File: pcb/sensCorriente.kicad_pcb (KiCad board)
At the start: 2 copper layers, 29 parts, among them J1 I_in, J2 USB, J3 SD-CON, J4 DB9, P1 LPCXpresso, SW1 CALIB, U1 ACS713, U2 MAX232

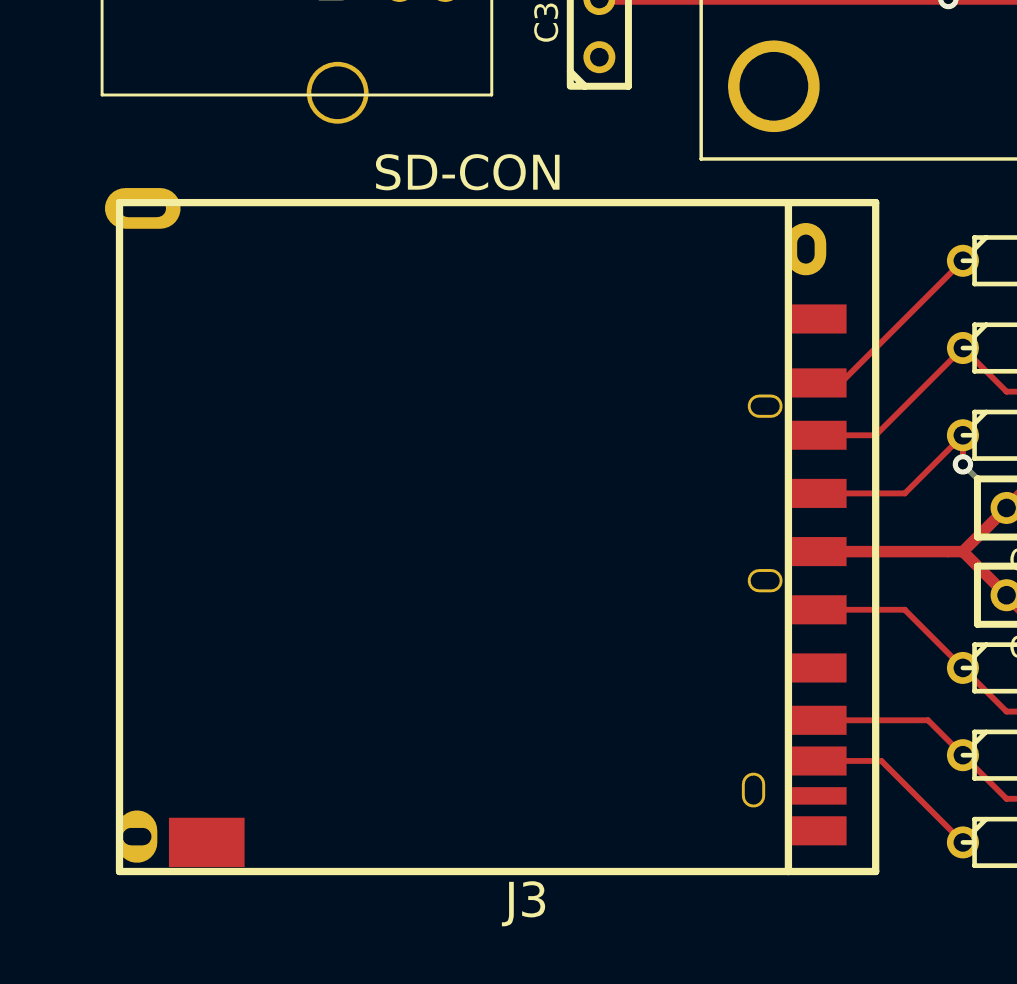
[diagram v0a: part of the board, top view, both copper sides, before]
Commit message: Se realizaron cambios en el esquematico. Revisar ERC.
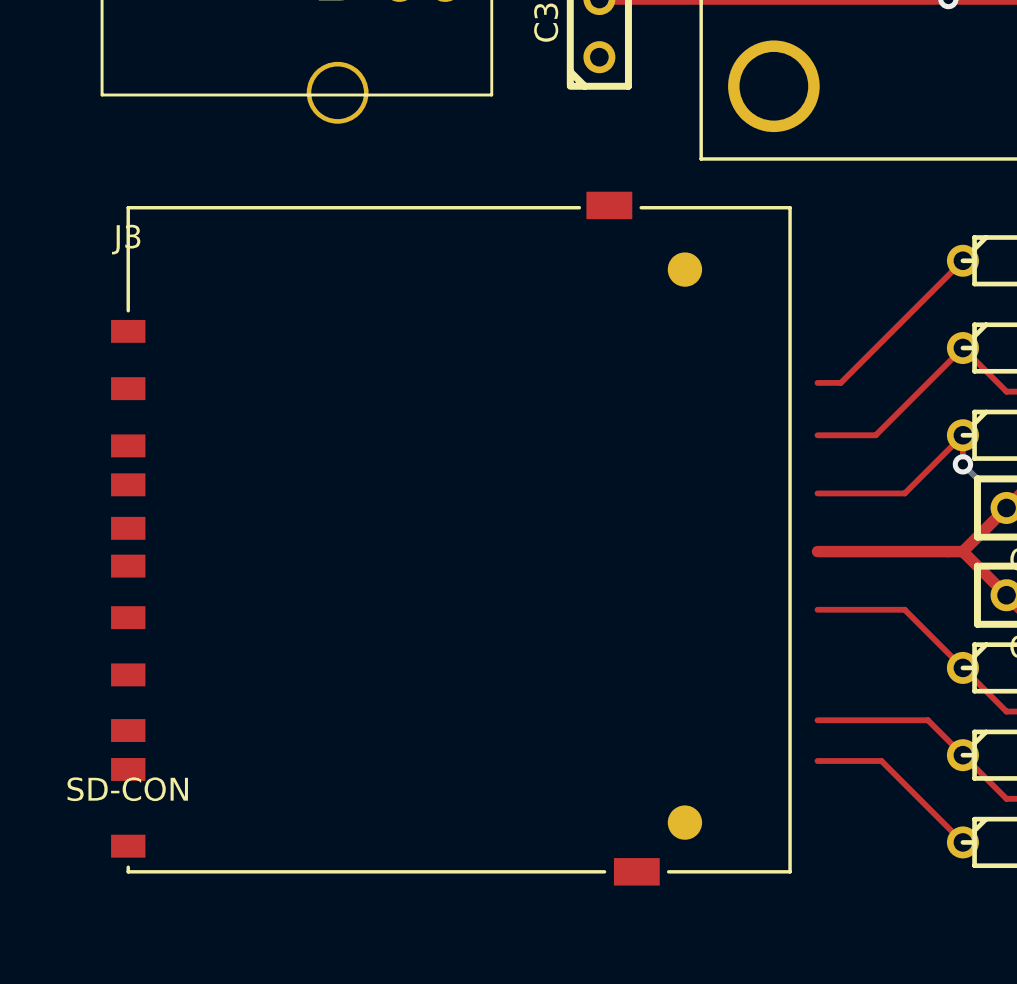
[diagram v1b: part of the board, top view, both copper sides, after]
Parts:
- J3: footprint SDCARD-REVERSE -> SD-CARD
- moved J3 30.4 mm to (124.2, 170.4), turned to 0 degrees
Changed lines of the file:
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@@
 (kicad_pcb (version 3) (host pcbnew "(2013-07-07 BZR 4022)-stable")
   (general
-    (links 90)
-    (no_connects 32)
+    (links 87)
+    (no_connects 36)
     (area 122.745499 115.443 308.381401 187.8584)
     (thickness 1.6)
@@
   )
   (setup
-    (last_trace_width 0.5)
+    (last_trace_width 0.254)
     (user_trace_width 0.5)
     (user_trace_width 1)
@@
     )
   )
-  (module SDCARD-REVERSE (layer F.Cu)
-    (at 154.305 166.37 180)
-    (fp_text reference J3 (at 12.7 -20.32 180) (layer F.SilkS)
-      (effects (font (size 1.524 1.524) (thickness 0.3048)))
-    )
-    (fp_text value SD-CON (at 15.24 11.43 180) (layer F.SilkS)
-      (effects (font (size 1.524 1.524) (thickness 0.3048)))
-    )
-    (fp_line (start 1.27 -19.05) (end -2.54 -19.05) (layer F.SilkS) (width 0.3175))
-    (fp_line (start -2.54 -19.05) (end -2.54 10.16) (layer F.SilkS) (width 0.3175))
-    (fp_line (start -2.54 10.16) (end 1.27 10.16) (layer F.SilkS) (width 0.3175))
-    (fp_line (start 30.48 -19.05) (end 1.27 -19.05) (layer F.SilkS) (width 0.3175))
-    (fp_line (start 1.27 -19.05) (end 1.27 10.16) (layer F.SilkS) (width 0.3175))
-    (fp_line (start 30.48 10.16) (end 1.27 10.16) (layer F.SilkS) (width 0.3175))
-    (fp_line (start 30.48 -19.05) (end 30.48 10.16) (layer F.SilkS) (width 0.3175))
-    (pad 9 smd rect (at 0 5.08 180) (size 2.54 1.27)
-      (layers F.Cu F.Paste F.Mask)
-      (net 21 GND)
-    )
-    (pad 1 smd rect (at 0 2.286 180) (size 2.54 1.27)
-      (layers F.Cu F.Paste F.Mask)
-      (net 23 N-0000025)
-    )
-    (pad 2 smd rect (at 0 0 180) (size 2.54 1.27)
-      (layers F.Cu F.Paste F.Mask)
-      (net 17 /SD_SSEL)
-    )
-    (pad 3 smd rect (at 0 -2.54 180) (size 2.54 1.27)
-      (layers F.Cu F.Paste F.Mask)
-      (net 16 /SD_MOSI)
-    )
-    (pad 4 smd rect (at 0 -5.08 180) (size 2.54 1.27)
-      (layers F.Cu F.Paste F.Mask)
-      (net 1 +3.3V)
-    )
-    (pad 5 smd rect (at 0 -7.62 180) (size 2.54 1.27)
-      (layers F.Cu F.Paste F.Mask)
-      (net 14 /SD_CLK)
-    )
-    (pad 6 smd rect (at 0 -10.16 180) (size 2.54 1.27)
-      (layers F.Cu F.Paste F.Mask)
-      (net 21 GND)
-    )
-    (pad 10 smd rect (at 0 -15.748 180) (size 2.54 0.762)
-      (layers F.Cu F.Paste F.Mask)
-      (net 21 GND)
-    )
-    (pad 8 smd rect (at 0 -14.224 180) (size 2.54 1.27)
-      (layers F.Cu F.Paste F.Mask)
-      (net 22 N-0000024)
-    )
-    (pad 11 smd rect (at 0 -17.272 180) (size 2.54 1.27)
-      (layers F.Cu F.Paste F.Mask)
-      (net 21 GND)
-    )
-    (pad 13 thru_hole oval (at 2.794 -15.494 180) (size 1.016 1.524) (drill oval 0.762 1.27)
-      (layers *.Cu *.Mask F.SilkS)
-    )
-    (pad 15 thru_hole oval (at 2.286 1.27 180) (size 1.524 1.016) (drill oval 1.27 0.762)
-      (layers *.Cu *.Mask F.SilkS)
-    )
-    (pad 16 thru_hole oval (at 0.508 8.128 180) (size 1.778 2.286) (drill oval 0.762 1.27)
-      (layers *.Cu *.Mask F.SilkS)
-    )
-    (pad 14 thru_hole oval (at 2.286 -6.35 180) (size 1.524 1.016) (drill oval 1.27 0.762)
-      (layers *.Cu *.Mask F.SilkS)
-    )
-    (pad 18 thru_hole oval (at 29.718 -17.526 180) (size 1.778 2.286) (drill oval 1.27 0.762)
-      (layers *.Cu *.Mask F.SilkS)
-    )
-    (pad 17 thru_hole oval (at 29.464 9.906 180) (size 3.302 1.778) (drill oval 2.032 0.762)
-      (layers *.Cu *.Mask F.SilkS)
-    )
-    (pad 7 smd rect (at 0 -12.446 180) (size 2.54 1.27)
-      (layers F.Cu F.Paste F.Mask)
-      (net 15 /SD_MISO)
-    )
-    (pad 12 smd rect (at 26.67 -17.78 180) (size 3.302 2.159)
-      (layers F.Cu F.Paste F.Mask)
-      (net 21 GND)
-    )
-  )
   (module RV2X4 (layer F.Cu)
     (at 258.445 124.46 270)
@@
       (scale (xyz 1 1 1))
       (rotate (xyz 0 0 0))
+    )
+  )
+  (module SD-CARD (layer F.Cu)
+    (at 124.206 170.434)
+    (fp_text reference J3 (at 0 -12.7) (layer F.SilkS)
+      (effects (font (size 1 1) (thickness 0.15)))
+    )
+    (fp_text value SD-CON (at 0 11.43) (layer F.SilkS)
+      (effects (font (size 1 1) (thickness 0.15)))
+    )
+    (fp_line (start 19.7 -14) (end 0 -14) (layer F.SilkS) (width 0.15))
+    (fp_line (start 28.9 15) (end 23.6 15) (layer F.SilkS) (width 0.15))
+    (fp_line (start 20.8 15) (end 0 15) (layer F.SilkS) (width 0.15))
+    (fp_line (start 0 15) (end 0 14.8) (layer F.SilkS) (width 0.15))
+    (fp_line (start 0 -14) (end 0 -9.5) (layer F.SilkS) (width 0.15))
+    (fp_line (start 28.9 -14) (end 28.9 15) (layer F.SilkS) (width 0.15))
+    (fp_line (start 22.4 -14) (end 28.9 -14) (layer F.SilkS) (width 0.15))
+    (pad 3 smd rect (at 0 0) (size 1.5 1)
+      (layers F.Cu F.Paste F.Mask)
+      (net 16 /SD_MOSI)
+    )
+    (pad 9 smd rect (at 0 -8.6) (size 1.5 1)
+      (layers F.Cu F.Paste F.Mask)
+      (net 21 GND)
+    )
+    (pad 2 smd rect (at 0 -3.6) (size 1.5 1)
+      (layers F.Cu F.Paste F.Mask)
+      (net 17 /SD_SSEL)
+    )
+    (pad CD smd rect (at 0 -1.9) (size 1.5 1)
+      (layers F.Cu F.Paste F.Mask)
+    )
+    (pad "" np_thru_hole circle (at 24.31 -11.3) (size 1.5 1.5)
+      (layers *.Cu *.Mask F.SilkS)
+    )
+    (pad 5 smd rect (at 0 3.9) (size 1.5 1)
+      (layers F.Cu F.Paste F.Mask)
+      (net 14 /SD_CLK)
+    )
+    (pad 4 smd rect (at 0 1.65) (size 1.5 1)
+      (layers F.Cu F.Paste F.Mask)
+      (net 1 +3.3V)
+    )
+    (pad 6 smd rect (at 0 6.4) (size 1.5 1)
+      (layers F.Cu F.Paste F.Mask)
+      (net 21 GND)
+    )
+    (pad 1 smd rect (at 0 -6.1) (size 1.5 1)
+      (layers F.Cu F.Paste F.Mask)
+      (net 23 N-0000025)
+    )
+    (pad WP smd rect (at 0 13.88) (size 1.5 1)
+      (layers F.Cu F.Paste F.Mask)
+    )
+    (pad "" np_thru_hole circle (at 24.31 12.85) (size 1.5 1.5)
+      (layers *.Cu *.Mask F.SilkS)
+    )
+    (pad 8 smd rect (at 0 10.53) (size 1.5 1)
+      (layers F.Cu F.Paste F.Mask)
+      (net 22 N-0000024)
+    )
+    (pad 7 smd rect (at 0 8.83) (size 1.5 1)
+      (layers F.Cu F.Paste F.Mask)
+      (net 15 /SD_MISO)
+    )
+    (pad GND smd rect (at 21.01 -14.1) (size 2 1.2)
+      (layers F.Cu F.Paste F.Mask)
+    )
+    (pad GND smd rect (at 22.21 15) (size 2 1.2)
+      (layers F.Cu F.Paste F.Mask)
     )
   )
@@
   (segment (start 154.305 168.91) (end 158.115 168.91) (width 0.254) (layer F.Cu) (net 16))
   (segment (start 158.115 168.91) (end 160.655 166.37) (width 0.254) (layer F.Cu) (net 16))
+  (segment (start 154.305 166.37) (end 156.845 166.37) (width 0.254) (layer F.Cu) (net 17))
   (segment (start 160.655 162.56) (end 162.56 164.465) (width 0.254) (layer F.Cu) (net 17))
   (segment (start 196.215 182.245) (end 196.215 183.515) (width 0.254) (layer F.Cu) (net 17))
@@
   (via (at 167.005 164.465) (size 0.889) (layers F.Cu B.Cu) (net 17))
   (segment (start 162.56 164.465) (end 167.005 164.465) (width 0.254) (layer F.Cu) (net 17))
-  (segment (start 154.305 166.37) (end 156.845 166.37) (width 0.254) (layer F.Cu) (net 17))
   (segment (start 156.845 166.37) (end 160.655 162.56) (width 0.254) (layer F.Cu) (net 17))
   (segment (start 208.915 183.515) (end 223.266 169.164) (width 0.254) (layer F.Cu) (net 18))

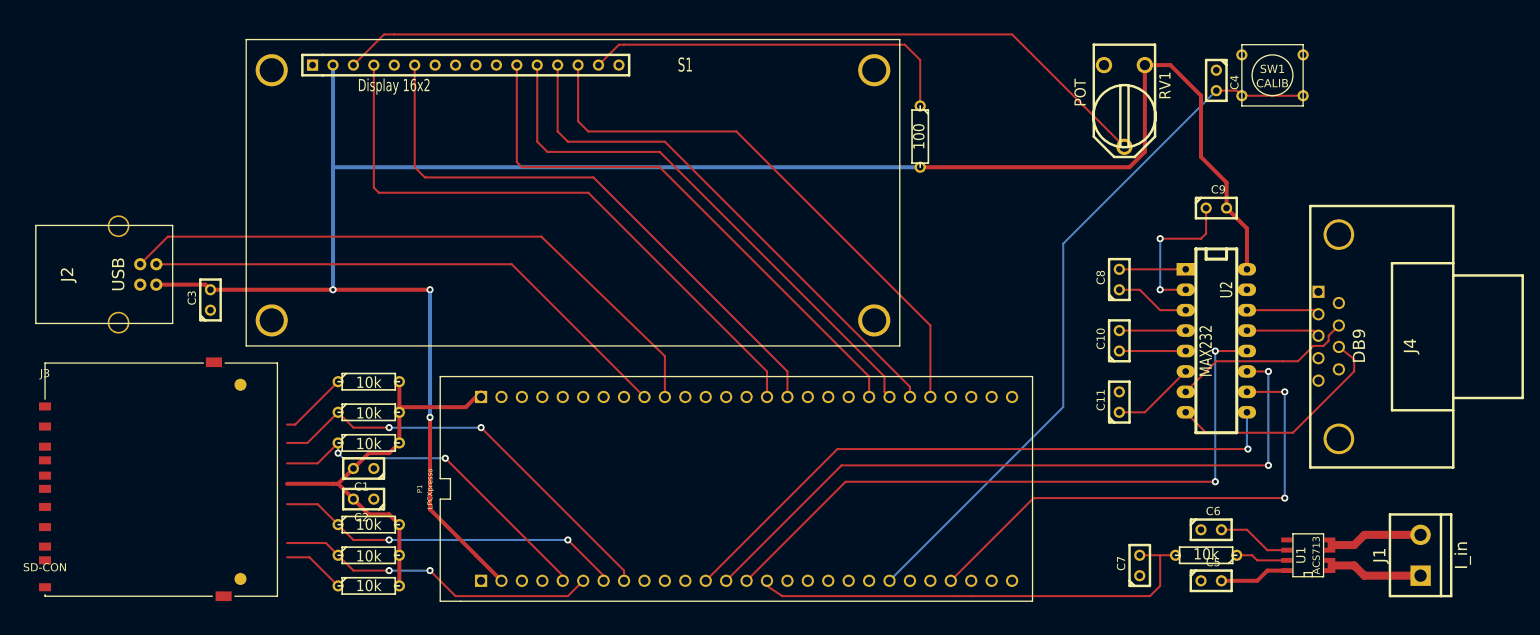
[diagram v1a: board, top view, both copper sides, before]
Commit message: Primer version del pcb terminado. Verificar y realizar correcciones. ERC OK en el esquematico y en el pcb.
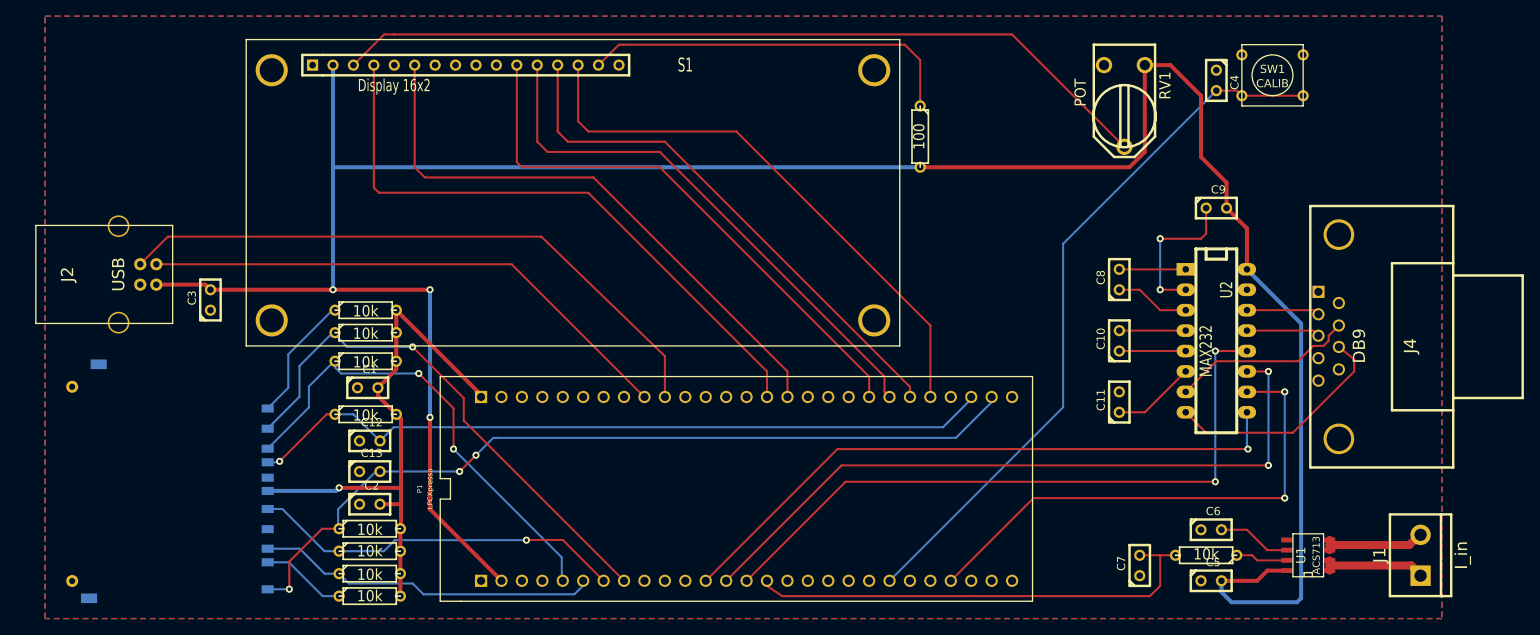
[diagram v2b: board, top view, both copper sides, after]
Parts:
- added C12: 100nF, C1, F.Cu at (164.6, 166.1)
- added C13: 100nF, C1, F.Cu at (164.6, 169.9)
- added R10: 10k, R3, F.Cu at (164.6, 177.0)
- added R9: 10k, R3, F.Cu at (164.1, 162.8)
- J3: value SD-CON -> CONECTORSD; moved to B.Cu
- moved J3 27.7 mm to (151.9, 170.7), turned to 180 degrees
- moved R3 10.2 mm to (164.1, 156.2)
- moved C1 10.0 mm to (164.3, 159.5), turned to 0 degrees
- moved R4 9.91 mm to (164.1, 152.7)
- moved R6 8.90 mm to (164.1, 149.9)
- moved R2 3.30 mm to (164.6, 179.8)
- moved R1 2.29 mm to (164.6, 182.6)
- moved R5 1.28 mm to (164.6, 185.4)
- moved C2 0.99 mm to (164.6, 174.0), turned to 0 degrees
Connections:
- J3 pad 1: N-0000025 (its old number) -> /SD_SSEL
- J3 pad 2: /SD_SSEL -> /SD_MOSI
- J3 pad 3: /SD_MOSI -> GND
- J3 pad 9: GND -> N-0000033
- J4 pad 10: GND -> (no net)
- J4 pad 11: GND -> (no net)
- P1 pad 52: (no net) -> /SD_CD
- P1 pad 53: (no net) -> /SD_WP
- R6 pad 1: N-0000025 (its old number) -> N-0000033
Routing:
- net /SD_WP: track 0.00 -> 103.9 mm, vias 0 -> 3
- net /SD_CD: track 0.00 -> 94.4 mm, vias 0 -> 1
- net +5V: track 255.8 -> 311.6 mm
- net +3.3V: track 52.0 -> 73.2 mm, vias 0 -> 1
- net N-0000033: track 0.00 -> 16.2 mm
- net /SD_MOSI: track 43.6 -> 59.7 mm
- net /SD_SSEL: track 52.9 -> 66.1 mm, vias 2 -> 1
- net N-0000025 (its old number): track 8.56 -> 0.00 mm
- net /SD_CLK: track 43.7 -> 47.3 mm, vias 2 -> 1
- net N-0000026: track 7.82 -> 10.6 mm
- net /SD_MISO: track 40.4 -> 42.6 mm, vias 2 -> 0
- net N-0000065: track 12.6 -> 13.2 mm
- net N-0000064: track 12.6 -> 13.1 mm
- added copper zone on B.Cu, net GND
- added copper zone on F.Cu, net GND
